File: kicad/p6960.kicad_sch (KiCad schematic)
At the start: 14 parts, among them J1 Conn_02x08_Counter_Clockwise, J2 Conn_02x08_Counter_Clockwise, J3 Conn_02x08_Counter_Clockwise, J4 Conn_02x08_Counter_Clockwise, J5 Conn_02x04_Counter_Clockwise

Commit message: fix my mild dyslexia
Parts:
- C1: footprint Tek:P9660 -> Tek:P6960; symbol tek:P9660 -> tek:P6960
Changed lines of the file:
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@@
 	)
 	(symbol
-		(lib_id "tek:P9660")
+		(lib_id "tek:P6960")
 		(at 146.05 74.93 0)
 		(unit 1)
@@
 			)
 		)
-		(property "Footprint" "Tek:P9660"
+		(property "Footprint" "Tek:P6960"
 			(at 140.335 35.2368 0)
 			(effects

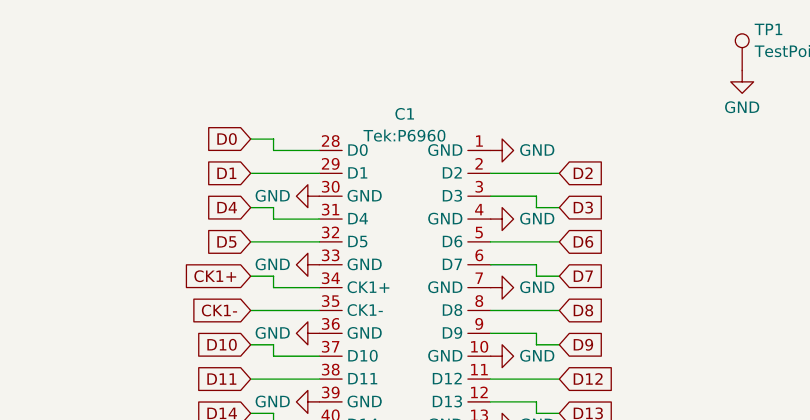
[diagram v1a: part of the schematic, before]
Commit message: tuned trace lengths
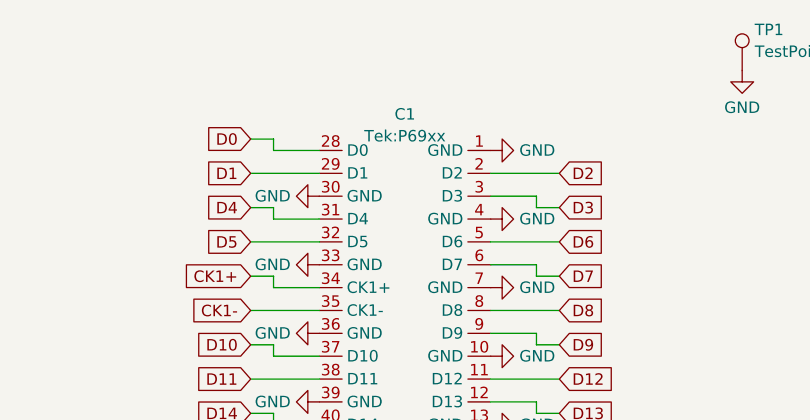
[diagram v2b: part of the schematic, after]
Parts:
- C1: footprint Tek:P6960 -> Tek:P69xx
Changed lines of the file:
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@@
 			)
 		)
-		(property "Footprint" "Tek:P6960"
+		(property "Footprint" "Tek:P69xx"
 			(at 140.335 35.2368 0)
 			(effects

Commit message: fixed some shite
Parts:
- C1: footprint Tek:P69xx -> Tek:P6960
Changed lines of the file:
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@@
 			)
 		)
-		(property "Footprint" "Tek:P69xx"
+		(property "Footprint" "Tek:P6960"
 			(at 140.335 35.2368 0)
 			(effects

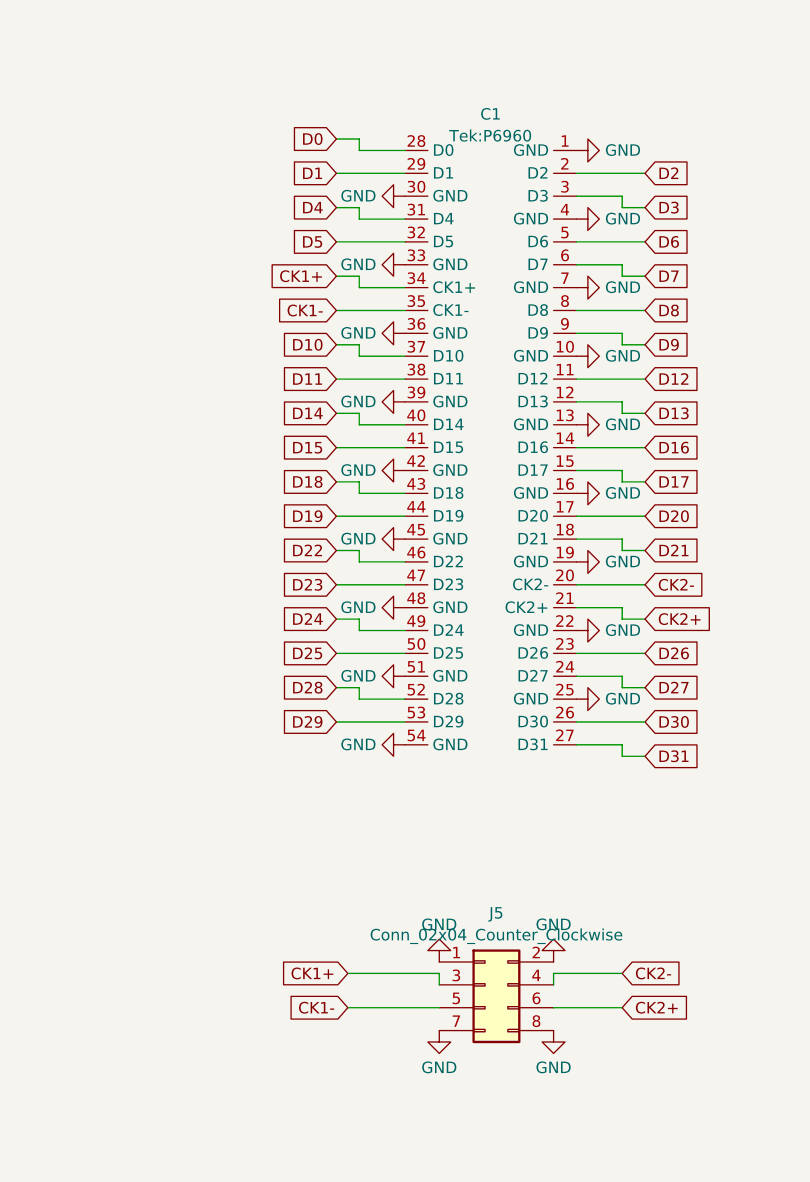
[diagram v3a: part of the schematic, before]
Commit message: Version 2.0
Changed header spacing, added real design rules (it fails), tuned all trace lengths to be 38mm, flood fill ground plane, added probe holder model, and more!
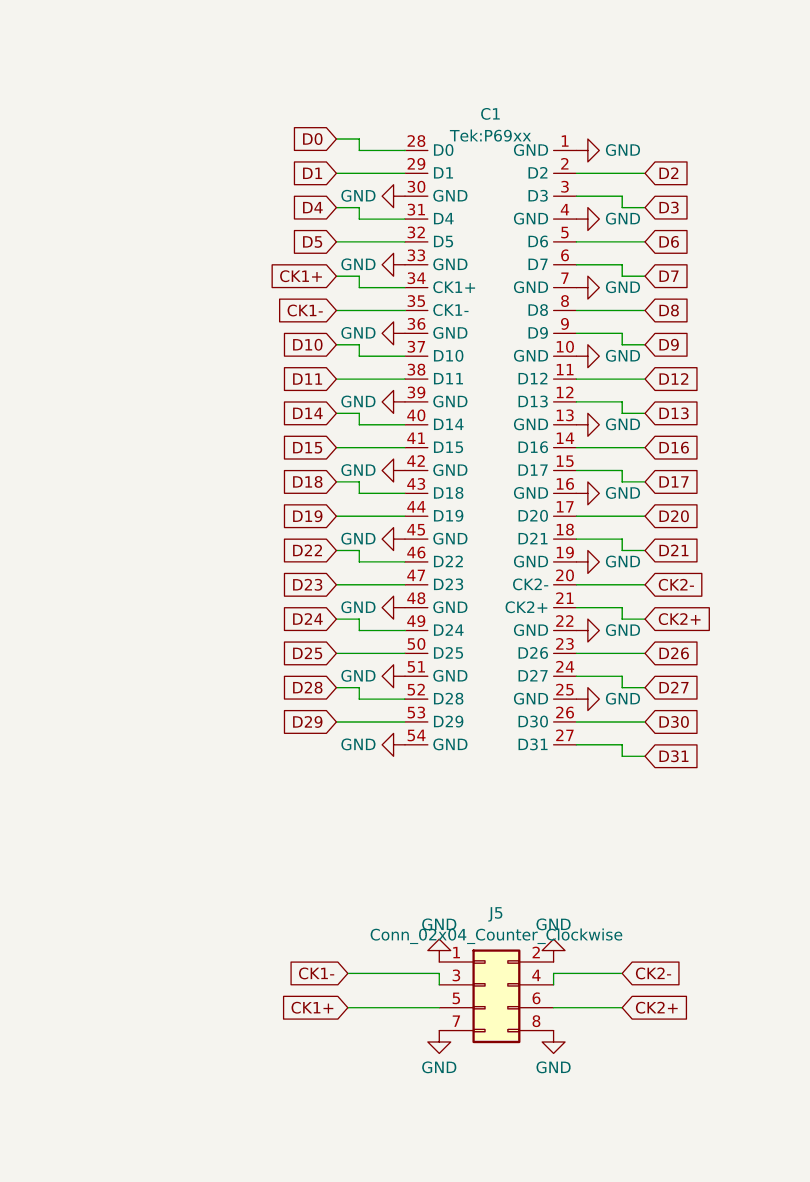
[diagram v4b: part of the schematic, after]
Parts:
- C1: footprint Tek:P6960 -> Tek:P69xx
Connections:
- net CK1+: now also J5.5 (Pin_5); no longer J5.3 (Pin_3)
- net CK1-: now also J5.3 (Pin_3); no longer J5.5 (Pin_5)
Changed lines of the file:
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@@
 		)
 	)
-	(global_label "CK1+"
+	(global_label "CK1-"
 		(shape input)
 		(at 124.46 128.27 180)
@@
 		)
 	)
-	(global_label "CK1-"
+	(global_label "CK1+"
 		(shape input)
 		(at 124.46 132.08 180)
@@
 			)
 		)
-		(property "Footprint" "Tek:P6960"
+		(property "Footprint" "Tek:P69xx"
 			(at 140.335 35.2368 0)
 			(effects
